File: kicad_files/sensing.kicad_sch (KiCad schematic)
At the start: 21 parts, among them Q3 AO3400A, U2 INA180A4, U3 INA180A4

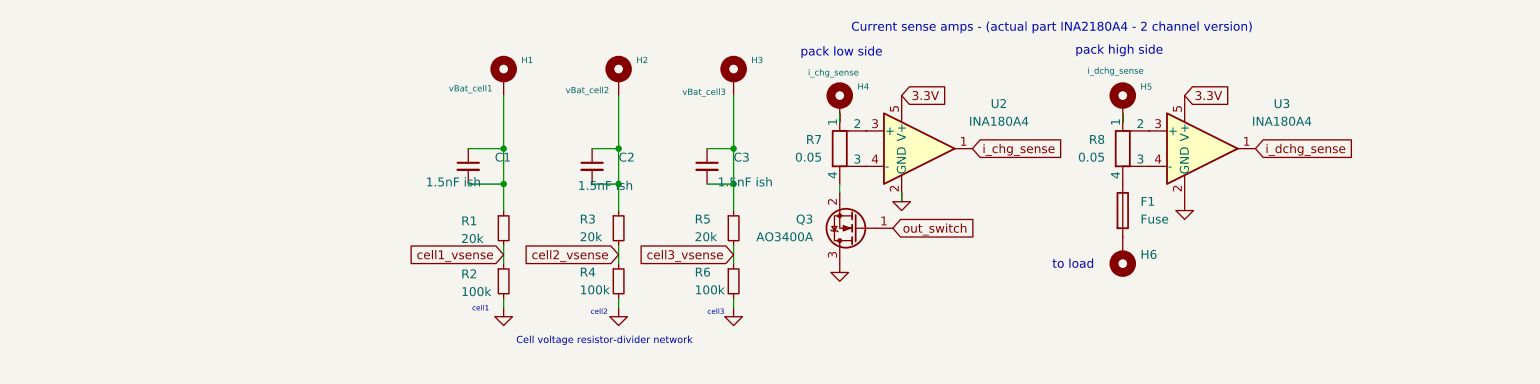
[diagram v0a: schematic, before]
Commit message: trying to add ina2180 footprint and symbol but didn't succed on footprint
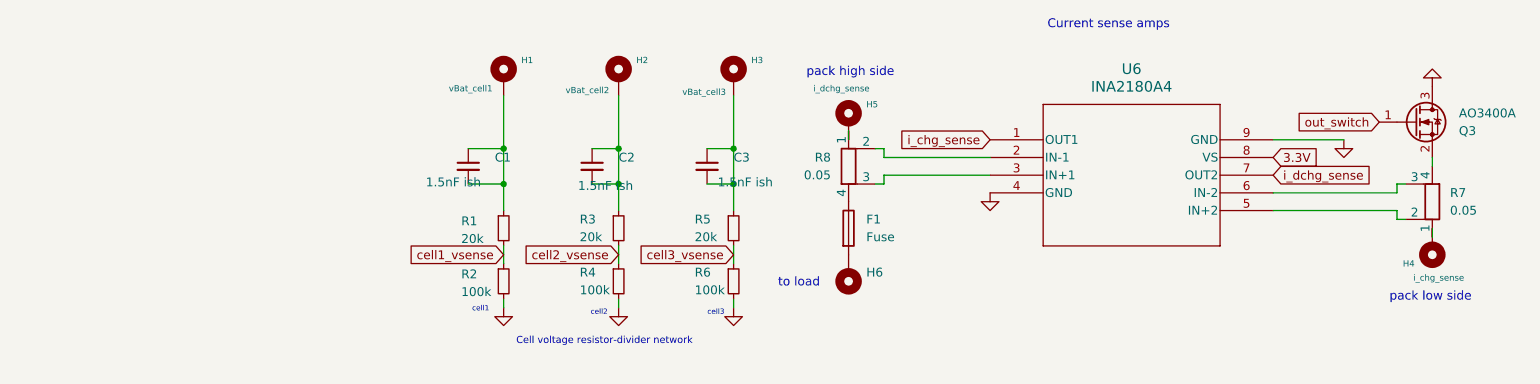
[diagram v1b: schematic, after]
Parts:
- removed U2, U3: INA180A4, Package_TO_SOT_SMD:SOT-23-5, symbol Amplifier_Current:INA180A4
- added U6: INA2180A4, WSON8_DSG_TEX, symbol 2026-06-15_08-03-52:INA2180A1IDSGR
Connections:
- net 3.3V: now also U6.8 (VS)
- net GND: now also U6.4 (GND), U6.9 (GND)
- net i_chg_sense: now also U6.1 (OUT1)
- net i_dchg_sense: now also U6.7 (OUT2)
- net at R8.2: now also U6.2 (IN-1)
- net at R8.3: now also U6.3 (IN+1)
- net at R7.2: now also U6.5 (IN+2)
- net at R7.3: now also U6.6 (IN-2)
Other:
- note added: "Current sense amps"
- note removed: "Current sense amps - (actual part INA2180A4 - 2 channel version)"
- moved on the sheet: F1, H4, H5, H6, Q3, R7, R8

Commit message: got footprint for current sense amp working
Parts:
- U6: footprint WSON8_DSG_TEX -> sodiumBMS_extras:WSON8_DSG_TEX
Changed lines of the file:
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@@
 			)
 		)
-		(property "Footprint" "WSON8_DSG_TEX"
+		(property "Footprint" "sodiumBMS_extras:WSON8_DSG_TEX"
 			(at 167.64 95.25 0)
 			(hide yes)

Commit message: more laying out
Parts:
- added R19: 10k, symbol Device:R_Small
- added TH1: 10k, symbol Device:Thermistor_NTC
- C1, C2, C3: footprint (none) -> Capacitor_SMD:C_0805_2012Metric_Pad1.18x1.45mm_HandSolder
- F1: footprint (none) -> Fuse:Fuseholder_Clip-5x20mm_Eaton_1A5601-01_Inline_P20.80x6.76mm_D1.70mm_Horizontal
- R1, R2, R7, R8: footprint (none) -> Resistor_SMD:R_0805_2012Metric_Pad1.20x1.40mm_HandSolder
- R3: value 20k -> 40k; footprint (none) -> Resistor_SMD:R_0805_2012Metric_Pad1.20x1.40mm_HandSolder
- R4, R6: value 100k -> 20k; footprint (none) -> Resistor_SMD:R_0805_2012Metric_Pad1.20x1.40mm_HandSolder
- R5: value 20k -> 60k; footprint (none) -> Resistor_SMD:R_0805_2012Metric_Pad1.20x1.40mm_HandSolder
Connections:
- net 3.3V: now also R19.1
- net GND: now also TH1.2
- new net temp_sense: R19.2, TH1.1

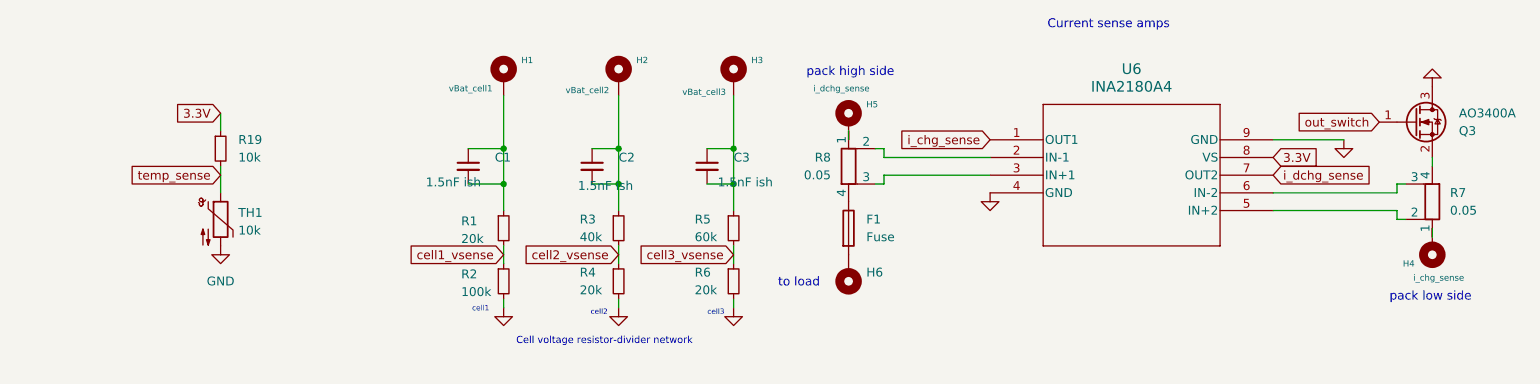
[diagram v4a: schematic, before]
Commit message: Fix sensing schematic and update main schematic
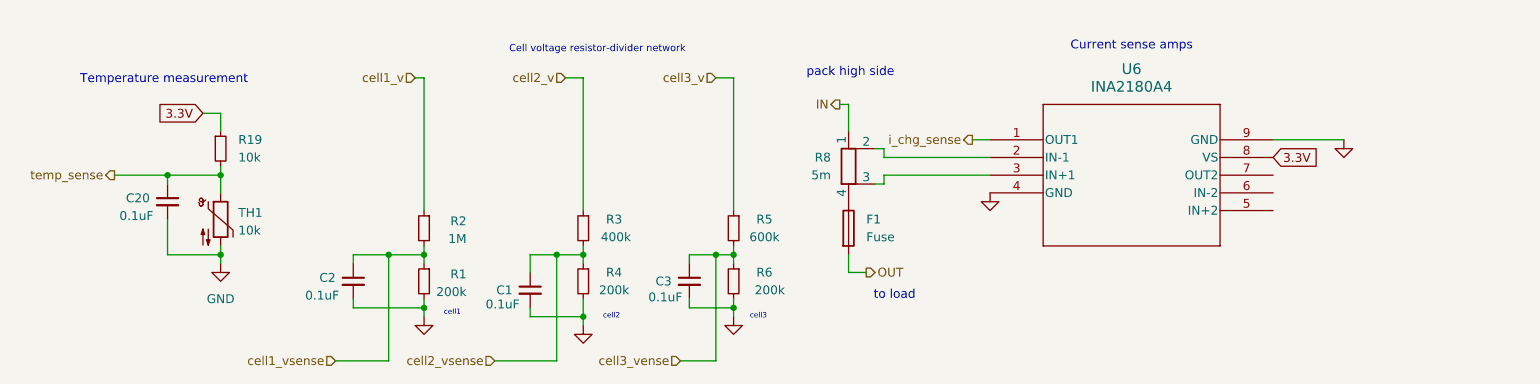
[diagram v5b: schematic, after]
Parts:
- removed H1: vBat_cell1, symbol Mechanical:MountingHole_Pad
- removed H2: vBat_cell2, symbol Mechanical:MountingHole_Pad
- removed H3: vBat_cell3, symbol Mechanical:MountingHole_Pad
- removed H4: i_chg_sense, symbol Mechanical:MountingHole_Pad
- removed H5: i_dchg_sense, symbol Mechanical:MountingHole_Pad
- removed H6: MountingHole_Pad, symbol Mechanical:MountingHole_Pad
- removed Q3: AO3400A, Package_TO_SOT_SMD:SOT-23, symbol Transistor_FET:AO3400A
- removed R7: 0.05, Resistor_SMD:R_0805_2012Metric_Pad1.20x1.40mm_HandSolder, symbol Device:R_Shunt
- added C20: 0.1uF, symbol Device:C_Small
- C1, C2, C3: value 1.5nF ish -> 0.1uF; footprint Capacitor_SMD:C_0805_2012Metric_Pad1.18x1.45mm_HandSolder -> (none)
- R1, R4, R6: value 20k -> 200k
- R2: value 100k -> 1M
- R3: value 40k -> 400k
- R5: value 60k -> 600k
- R8: value 0.05 -> 5m
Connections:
- net GND: now also C1.2, C2.2, C3.2, R1.2, C20.2; no longer R2.2
- net cell1_vsense: now also C2.1, R1.1, R2.2; no longer R1.2, R2.1
- net cell2_vsense: now also C1.1
- net temp_sense: now also C20.1
- net OUT: now reaches F1.2
- net IN: now reaches R8.1
- net cell3_vsense renamed cell3_vense
- net cell3_vense: now also C3.1
- net i_dchg_sense: no longer names the net of U6.7 (OUT2)
- new net cell1_v: R2.1
- new net cell2_v: R3.1
- new net cell3_v: R5.1
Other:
- note added: "Temperature measurement"
- note removed: "pack low side"
- moved on the sheet: R1, R2, R3, R4

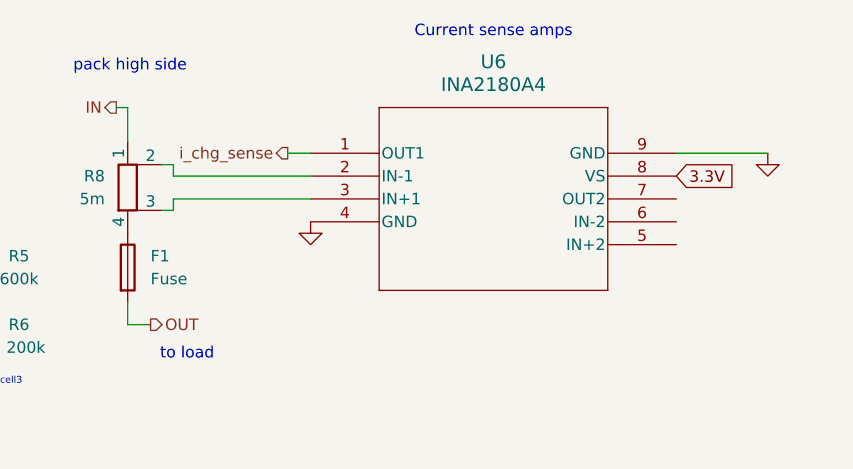
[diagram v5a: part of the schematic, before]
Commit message: Add discharge current measurement
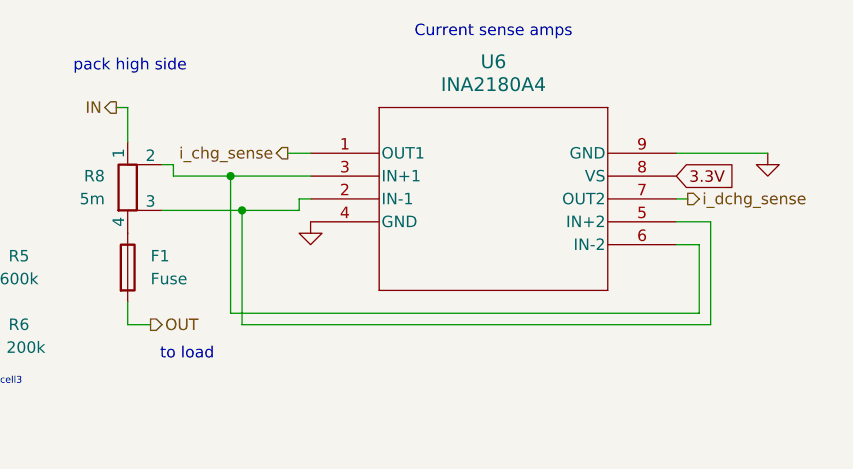
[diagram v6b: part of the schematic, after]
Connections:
- net at R8.2: now also U6.3 (IN+1), U6.6 (IN-2); no longer U6.2 (IN-1)
- net at R8.3: now also U6.2 (IN-1), U6.5 (IN+2); no longer U6.3 (IN+1)
- net i_dchg_sense: now reaches U6.7 (OUT2)
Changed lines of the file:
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@@
+	)
+	(junction
+		(at 160.02 101.6)
+		(diameter 0)
+		(color 0 0 0 0)
 	)
 	(junction
@@
 	)
 	(junction
+		(at 158.75 97.79)
+		(diameter 0)
+		(color 0 0 0 0)
+	)
+	(junction
 		(at 86.36 119.38)
 		(diameter 0)
@@
 	(wire
 		(pts
+			(xy 208.28 100.33) (xy 209.55 100.33)
+		)
+		(stroke
+			(width 0)
+			(type default)
+		)
+	)
+	(wire
+		(pts
+			(xy 151.13 101.6) (xy 160.02 101.6)
+		)
+		(stroke
+			(width 0)
+			(type default)
+		)
+	)
+	(wire
+		(pts
+			(xy 210.82 113.03) (xy 210.82 105.41)
+		)
+		(stroke
+			(width 0)
+			(type default)
+		)
+	)
+	(wire
+		(pts
 			(xy 130.81 86.36) (xy 130.81 105.41)
 		)
@@
 	(wire
 		(pts
+			(xy 160.02 101.6) (xy 166.37 101.6)
+		)
+		(stroke
+			(width 0)
+			(type default)
+		)
+	)
+	(wire
+		(pts
 			(xy 109.22 86.36) (xy 109.22 105.41)
 		)
@@
 	(wire
 		(pts
+			(xy 160.02 114.3) (xy 160.02 101.6)
+		)
+		(stroke
+			(width 0)
+			(type default)
+		)
+	)
+	(wire
+		(pts
 			(xy 124.46 119.38) (xy 130.81 119.38)
 		)
@@
 	(wire
 		(pts
+			(xy 158.75 97.79) (xy 167.64 97.79)
+		)
+		(stroke
+			(width 0)
+			(type default)
+		)
+	)
+	(wire
+		(pts
 			(xy 57.15 111.76) (xy 57.15 113.03)
 		)
@@
 	(wire
 		(pts
+			(xy 212.09 114.3) (xy 160.02 114.3)
+		)
+		(stroke
+			(width 0)
+			(type default)
+		)
+	)
+	(wire
+		(pts
 			(xy 124.46 113.03) (xy 124.46 111.76)
 		)
@@
 	(wire
 		(pts
-			(xy 152.4 101.6) (xy 152.4 100.33)
-		)
-		(stroke
-			(width 0)
-			(type default)
-		)
-	)
-	(wire
-		(pts
 			(xy 130.81 111.76) (xy 130.81 113.03)
 		)
@@
 	(wire
 		(pts
+			(xy 210.82 105.41) (xy 208.28 105.41)
+		)
+		(stroke
+			(width 0)
+			(type default)
+		)
+	)
+	(wire
+		(pts
 			(xy 76.2 118.11) (xy 76.2 119.38)
 		)
@@
 	(wire
 		(pts
+			(xy 158.75 97.79) (xy 158.75 113.03)
+		)
+		(stroke
+			(width 0)
+			(type default)
+		)
+	)
+	(wire
+		(pts
 			(xy 57.15 100.33) (xy 57.15 102.87)
 		)
@@
 	(wire
 		(pts
-			(xy 151.13 101.6) (xy 152.4 101.6)
-		)
-		(stroke
-			(width 0)
-			(type default)
-		)
-	)
-	(wire
-		(pts
 			(xy 109.22 111.76) (xy 109.22 113.03)
 		)
@@
 	(wire
 		(pts
+			(xy 158.75 113.03) (xy 210.82 113.03)
+		)
+		(stroke
+			(width 0)
+			(type default)
+		)
+	)
+	(wire
+		(pts
 			(xy 57.15 91.44) (xy 57.15 93.98)
 		)
@@
 	(wire
 		(pts
+			(xy 166.37 101.6) (xy 166.37 100.33)
+		)
+		(stroke
+			(width 0)
+			(type default)
+		)
+	)
+	(wire
+		(pts
 			(xy 86.36 110.49) (xy 86.36 111.76)
 		)
@@
 	(wire
 		(pts
+			(xy 208.28 102.87) (xy 212.09 102.87)
+		)
+		(stroke
+			(width 0)
+			(type default)
+		)
+	)
+	(wire
+		(pts
 			(xy 57.15 110.49) (xy 57.15 111.76)
 		)
@@
 	(wire
 		(pts
+			(xy 212.09 102.87) (xy 212.09 114.3)
+		)
+		(stroke
+			(width 0)
+			(type default)
+		)
+	)
+	(wire
+		(pts
 			(xy 146.05 90.17) (xy 147.32 90.17)
 		)
@@
 	(wire
 		(pts
-			(xy 152.4 97.79) (xy 167.64 97.79)
+			(xy 152.4 97.79) (xy 158.75 97.79)
 		)
 		(stroke
@@
 	(wire
 		(pts
+			(xy 166.37 100.33) (xy 167.64 100.33)
+		)
+		(stroke
+			(width 0)
+			(type default)
+		)
+	)
+	(wire
+		(pts
 			(xy 49.53 101.6) (xy 49.53 100.33)
 		)
@@
 		(pts
 			(xy 86.36 118.11) (xy 86.36 119.38)
-		)
-		(stroke
-			(width 0)
-			(type default)
-		)
-	)
-	(wire
-		(pts
-			(xy 152.4 100.33) (xy 167.64 100.33)
 		)
 		(stroke
@@
 		)
 	)
+	(hierarchical_label "i_dchg_sense"
+		(shape output)
+		(at 209.55 100.33 0)
+		(effects
+			(font
+				(size 1.27 1.27)
+			)
+			(justify left)
+		)
+	)
